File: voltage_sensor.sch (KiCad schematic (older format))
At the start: 20 parts, among them K1 REF, P1 Input, P2 CONN_4, P3 CONN_2, U1 REF5020, U2 LT6011, U3 ADUM5401, U4 MCP3550

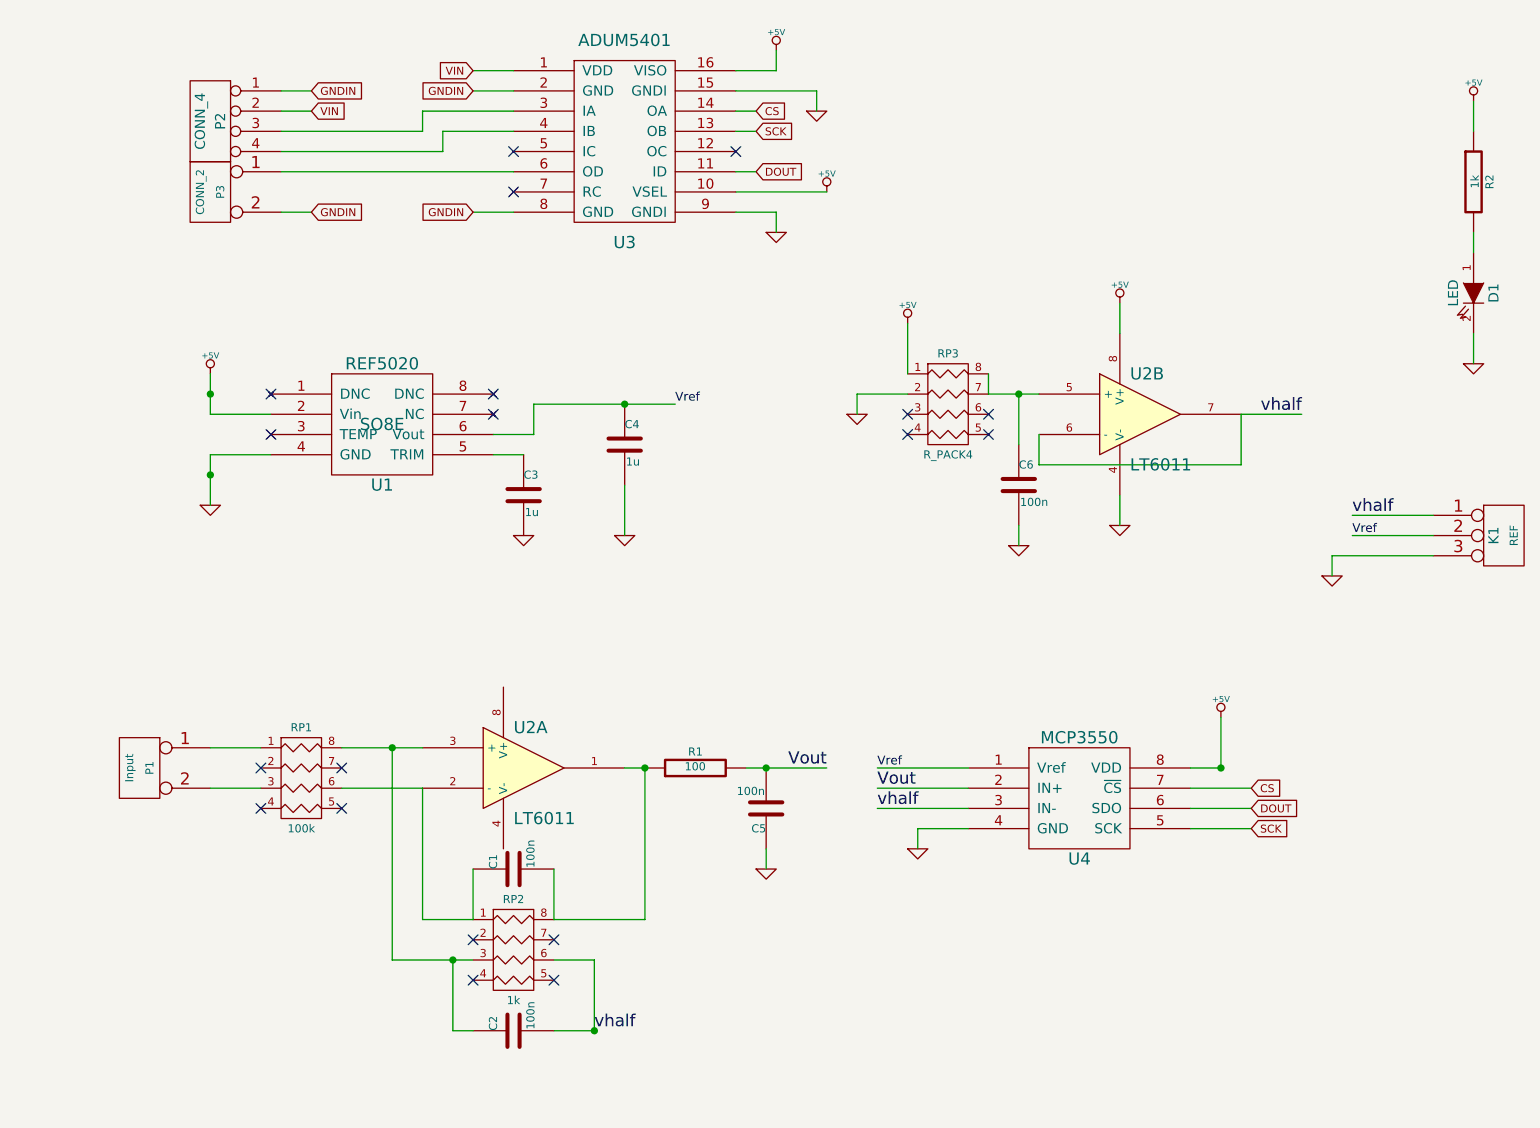
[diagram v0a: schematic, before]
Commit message: Started routing board
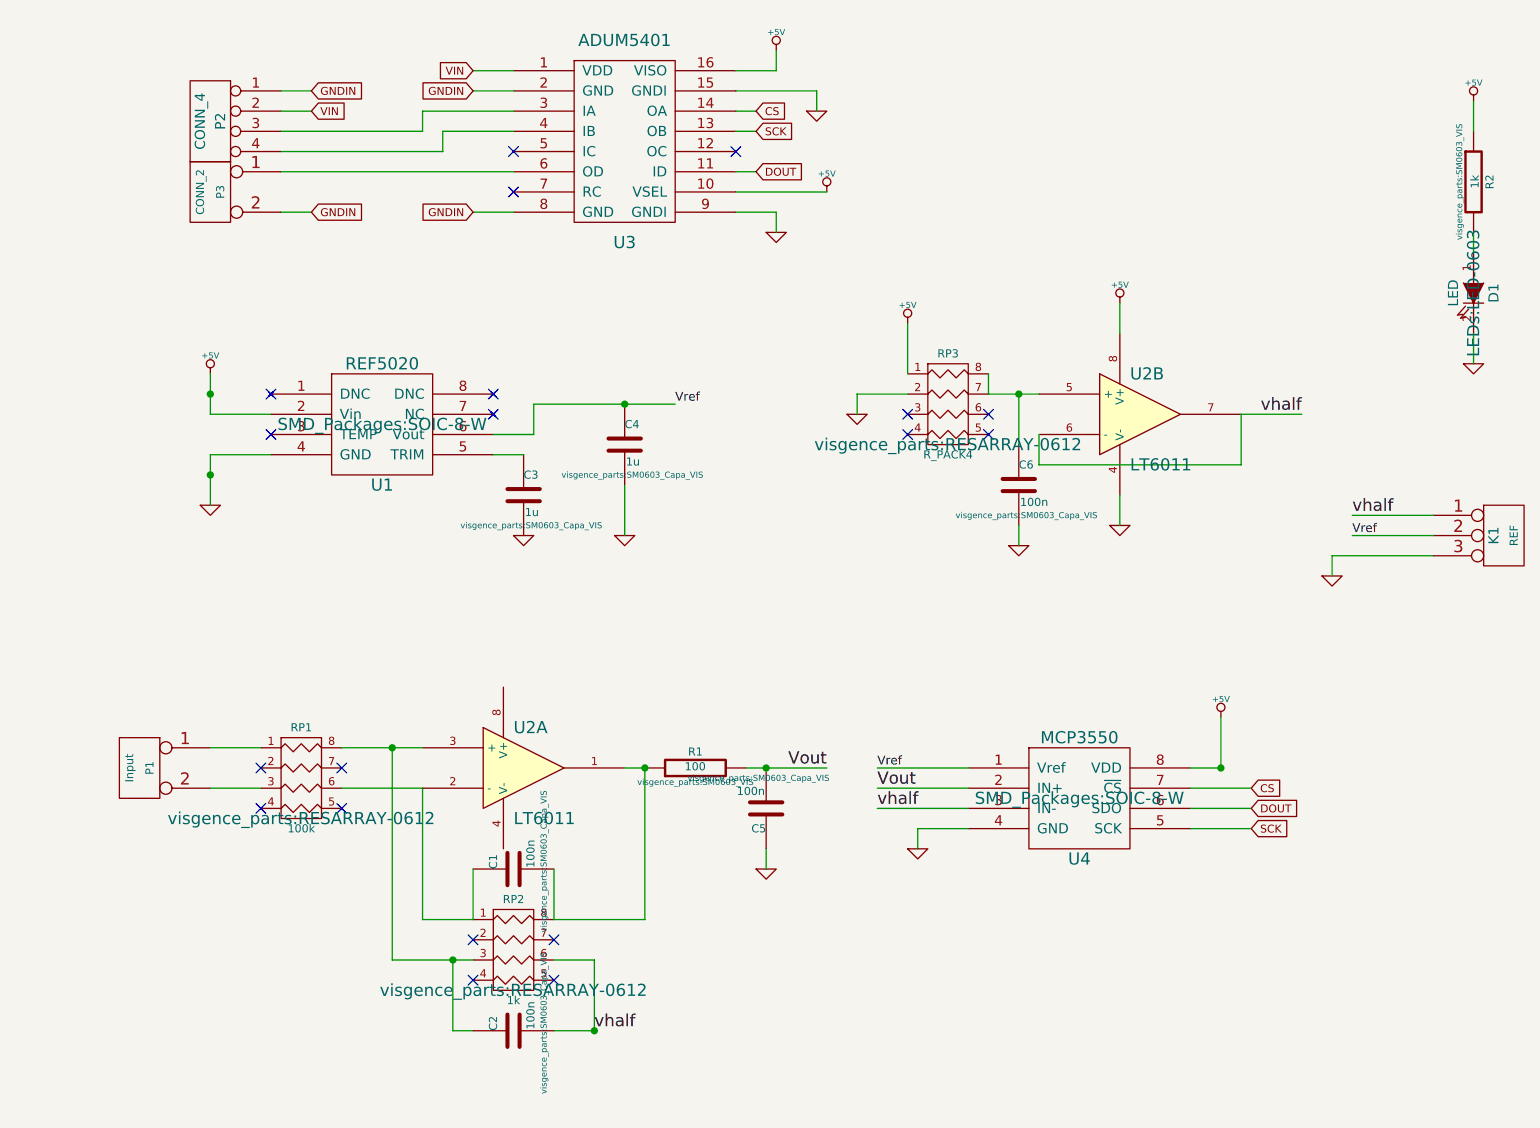
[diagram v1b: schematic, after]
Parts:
- C1, C2, C3, C4, C5, C6: footprint ~ -> visgence_parts:SM0603_Capa_VIS
- D1: footprint ~ -> LEDs:LED-0603
- K1: footprint (none) -> Pin_Headers:Pin_Header_Straight_1x03
- P1: footprint (none) -> Connect:bornier2
- P2: footprint (none) -> visgence_parts:Term3.5-4
- P3: footprint (none) -> visgence_parts:Term3.5-2
- R1, R2: footprint ~ -> visgence_parts:SM0603_VIS
- RP1, RP2, RP3: footprint ~ -> visgence_parts:RESARRAY-0612
- U1: footprint SO8E -> SMD_Packages:SOIC-8-W
- U2: footprint (none) -> SMD_Packages:SOIC-8-W
- U3: footprint (none) -> SMD_Packages:SO-16-W
- U4: footprint ~ -> SMD_Packages:SOIC-8-W
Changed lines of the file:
@@
 F 0 "C4" H 4050 3300 40  0000 L CNN
 F 1 "1u" H 4056 3115 40  0000 L CNN
-F 2 "~" H 4088 3050 30  0000 C CNN
+F 2 "visgence_parts:SM0603_Capa_VIS" H 4088 3050 30  0000 C CNN
 F 3 "~" H 4050 3200 60  0000 C CNN
 	1    4050 3200
@@
 F 0 "RP3" H 5650 3650 40  0000 C CNN
 F 1 "R_PACK4" H 5650 3150 40  0000 C CNN
-F 2 "~" H 5650 3200 60  0000 C CNN
+F 2 "visgence_parts:RESARRAY-0612" H 5650 3200 60  0000 C CNN
 F 3 "~" H 5650 3200 60  0000 C CNN
 	1    5650 3200
@@
 F 0 "C6" H 6000 3500 40  0000 L CNN
 F 1 "100n" H 6006 3315 40  0000 L CNN
-F 2 "~" H 6038 3250 30  0000 C CNN
+F 2 "visgence_parts:SM0603_Capa_VIS" H 6038 3250 30  0000 C CNN
 F 3 "~" H 6000 3400 60  0000 C CNN
 	1    6000 3400
@@
 F 0 "RP1" H 2450 5500 40  0000 C CNN
 F 1 "100k" H 2450 5000 40  0000 C CNN
-F 2 "~" H 2450 5050 60  0000 C CNN
+F 2 "visgence_parts:RESARRAY-0612" H 2450 5050 60  0000 C CNN
 F 3 "~" H 2450 5050 60  0000 C CNN
 	1    2450 5050
@@
 F 0 "RP2" H 3500 6350 40  0000 C CNN
 F 1 "1k" H 3500 5850 40  0000 C CNN
-F 2 "~" H 3500 5900 60  0000 C CNN
+F 2 "visgence_parts:RESARRAY-0612" H 3500 5900 60  0000 C CNN
 F 3 "~" H 3500 5900 60  0000 C CNN
 	1    3500 5900
@@
 F 0 "C1" H 3500 5400 40  0000 L CNN
 F 1 "100n" H 3506 5215 40  0000 L CNN
-F 2 "~" H 3538 5150 30  0000 C CNN
+F 2 "visgence_parts:SM0603_Capa_VIS" H 3538 5150 30  0000 C CNN
 F 3 "~" H 3500 5300 60  0000 C CNN
 	1    3500 5300
@@
 F 0 "C2" H 3500 6200 40  0000 L CNN
 F 1 "100n" H 3506 6015 40  0000 L CNN
-F 2 "~" H 3538 5950 30  0000 C CNN
+F 2 "visgence_parts:SM0603_Capa_VIS" H 3538 5950 30  0000 C CNN
 F 3 "~" H 3500 6100 60  0000 C CNN
 	1    3500 6100
@@
 F 0 "R1" V 4480 4800 40  0000 C CNN
 F 1 "100" V 4407 4801 40  0000 C CNN
-F 2 "~" V 4330 4800 30  0000 C CNN
+F 2 "visgence_parts:SM0603_VIS" V 4330 4800 30  0000 C CNN
 F 3 "~" H 4400 4800 30  0000 C CNN
 	1    4400 4800
@@
 F 0 "C5" H 4750 5100 40  0000 L CNN
 F 1 "100n" H 4756 4915 40  0000 L CNN
-F 2 "~" H 4788 4850 30  0000 C CNN
+F 2 "visgence_parts:SM0603_Capa_VIS" H 4788 4850 30  0000 C CNN
 F 3 "~" H 4750 5000 60  0000 C CNN
 	1    4750 5000
@@
 F 0 "P1" V 1600 4800 40  0000 C CNN
 F 1 "Input" V 1700 4800 40  0000 C CNN
-F 2 "" H 1650 4800 60  0000 C CNN
+F 2 "Connect:bornier2" H 1650 4800 60  0001 C CNN
 F 3 "" H 1650 4800 60  0000 C CNN
 	1    1650 4800
@@
 F 0 "D1" H 8250 2550 50  0000 C CNN
 F 1 "LED" H 8250 2350 50  0000 C CNN
-F 2 "~" H 8250 2450 60  0000 C CNN
+F 2 "LEDs:LED-0603" H 8250 2450 60  0000 C CNN
 F 3 "~" H 8250 2450 60  0000 C CNN
 	1    8250 2450
@@
 F 0 "R2" V 8330 1900 40  0000 C CNN
 F 1 "1k" V 8257 1901 40  0000 C CNN
-F 2 "~" V 8180 1900 30  0000 C CNN
+F 2 "visgence_parts:SM0603_VIS" V 8180 1900 30  0000 C CNN
 F 3 "~" H 8250 1900 30  0000 C CNN
 	1    8250 1900
@@
 F 0 "K1" V 8350 3650 50  0000 C CNN
 F 1 "REF" V 8450 3650 40  0000 C CNN
-F 2 "" H 8400 3650 60  0000 C CNN
+F 2 "Pin_Headers:Pin_Header_Straight_1x03" H 8400 3650 60  0001 C CNN
 F 3 "" H 8400 3650 60  0000 C CNN
 	1    8400 3650
@@
 F 0 "U2" H 6550 3250 60  0000 L CNN
 F 1 "LT6011" H 6550 2800 60  0000 L CNN
-F 2 "" H 6600 3050 60  0000 C CNN
+F 2 "SMD_Packages:SOIC-8-W" H 6600 3050 60  0001 C CNN
 F 3 "" H 6600 3050 60  0000 C CNN
 	2    6600 3050
@@
 F 0 "U1" H 2850 2800 60  0000 C CNN
 F 1 "REF5020" H 2850 3400 60  0000 C CNN
-F 2 "SO8E" H 2850 3100 60  0000 C CNN
+F 2 "SMD_Packages:SOIC-8-W" H 2850 3100 60  0000 C CNN
 F 3 "~" H 2850 3100 60  0000 C CNN
 	1    2850 3100
@@
 F 0 "U2" H 3500 5000 60  0000 L CNN
 F 1 "LT6011" H 3500 4550 60  0000 L CNN
-F 2 "" H 3550 4800 60  0000 C CNN
+F 2 "SMD_Packages:SOIC-8-W" H 3550 4800 60  0001 C CNN
 F 3 "" H 3550 4800 60  0000 C CNN
 	1    3550 4800
@@
 F 0 "U4" H 6300 4650 60  0000 C CNN
 F 1 "MCP3550" H 6300 5250 60  0000 C CNN
-F 2 "~" H 6300 4950 60  0000 C CNN
+F 2 "SMD_Packages:SOIC-8-W" H 6300 4950 60  0000 C CNN
 F 3 "~" H 6300 4950 60  0000 C CNN
 	1    6300 4950
@@
 F 0 "C3" H 3550 3550 40  0000 L CNN
 F 1 "1u" H 3556 3365 40  0000 L CNN
-F 2 "~" H 3588 3300 30  0000 C CNN
+F 2 "visgence_parts:SM0603_Capa_VIS" H 3588 3300 30  0000 C CNN
 F 3 "~" H 3550 3450 60  0000 C CNN
 	1    3550 3450
@@
 F 0 "U3" H 4050 1200 60  0000 C CNN
 F 1 "ADUM5401" H 4050 2200 60  0000 C CNN
-F 2 "" H 4050 1600 60  0000 C CNN
+F 2 "SMD_Packages:SO-16-W" H 4050 1600 60  0001 C CNN
 F 3 "" H 4050 1600 60  0000 C CNN
 	1    4050 1700
@@
 F 0 "P2" V 1950 1600 50  0000 C CNN
 F 1 "CONN_4" V 2050 1600 50  0000 C CNN
-F 2 "" H 2000 1600 60  0000 C CNN
+F 2 "visgence_parts:Term3.5-4" H 2000 1600 60  0001 C CNN
 F 3 "" H 2000 1600 60  0000 C CNN
 	1    2000 1600
@@
 F 0 "P3" V 1950 1950 40  0000 C CNN
 F 1 "CONN_2" V 2050 1950 40  0000 C CNN
-F 2 "" H 2000 1950 60  0000 C CNN
+F 2 "visgence_parts:Term3.5-2" H 2000 1950 60  0001 C CNN
 F 3 "" H 2000 1950 60  0000 C CNN
 	1    2000 1950

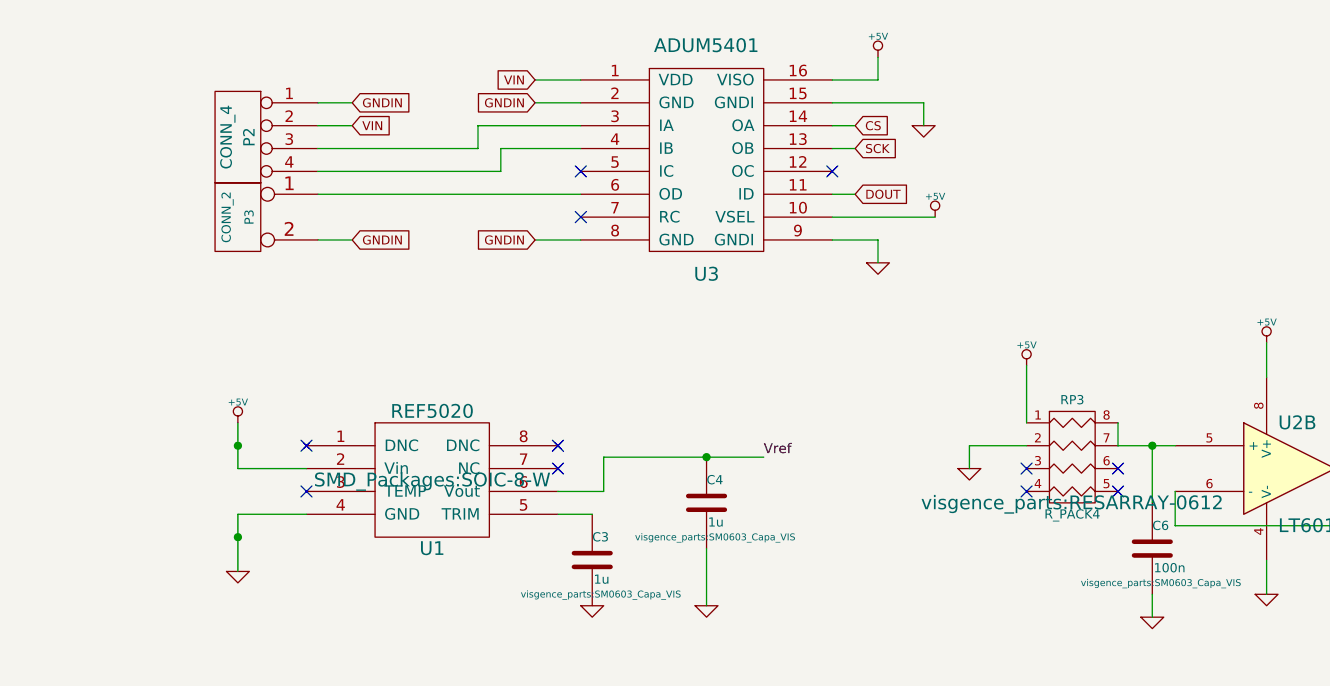
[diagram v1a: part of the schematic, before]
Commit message: Added filter caps
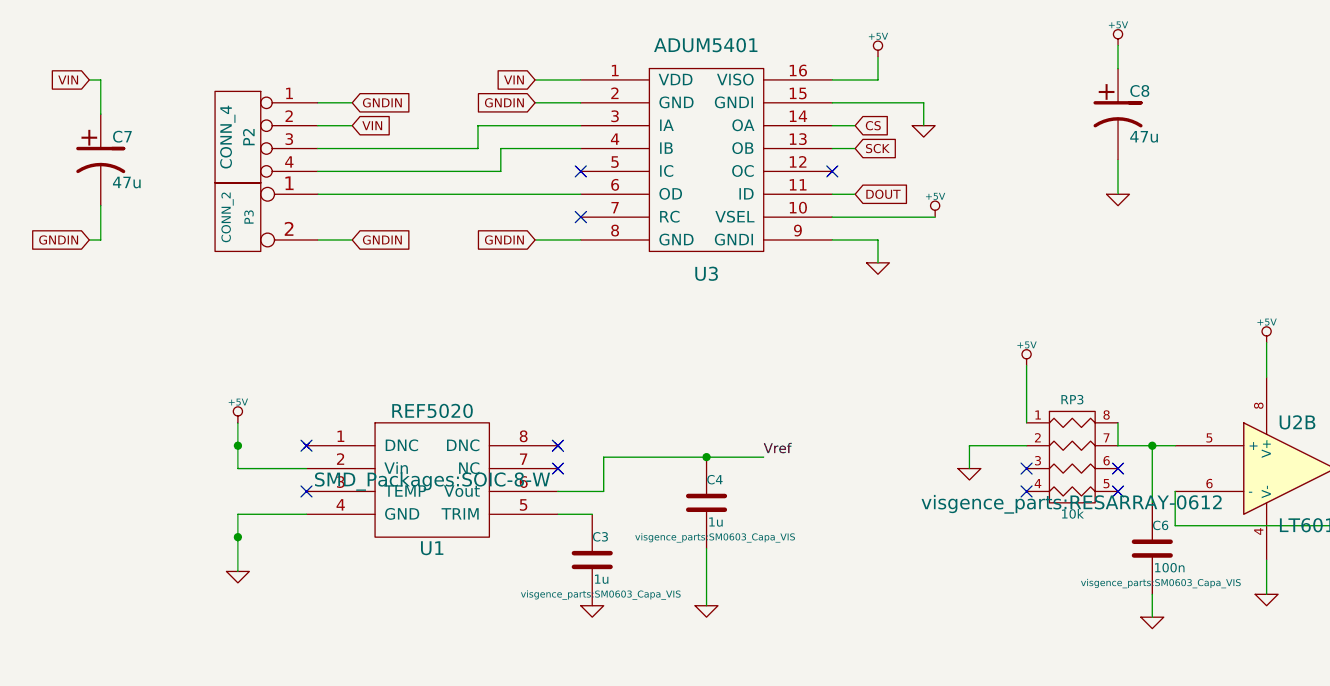
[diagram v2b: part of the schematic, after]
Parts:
- added C7, C8: 47u, visgence_parts:SM1206POL_VIS, symbol CP1
- RP3: value R_PACK4 -> 10k
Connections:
- net +5V: now also C8.1
- net GND: now also C8.2
- net GNDIN: now also C7.2
- net VIN: now also C7.1
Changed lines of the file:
@@
 P 5650 3200
 F 0 "RP3" H 5650 3650 40  0000 C CNN
-F 1 "R_PACK4" H 5650 3150 40  0000 C CNN
+F 1 "10k" H 5650 3150 40  0000 C CNN
 F 2 "visgence_parts:RESARRAY-0612" H 5650 3200 60  0000 C CNN
 F 3 "~" H 5650 3200 60  0000 C CNN
@@
 	3300 1350 3500 1350
 NoConn ~ 3500 1750
+$Comp
+L CP1 C8
+U 1 1 53EC4C40
+P 5850 1500
+F 0 "C8" H 5900 1600 50  0000 L CNN
+F 1 "47u" H 5900 1400 50  0000 L CNN
+F 2 "visgence_parts:SM1206POL_VIS" H 5850 1500 60  0001 C CNN
+F 3 "" H 5850 1500 60  0000 C CNN
+	1    5850 1500
+	1    0    0    -1
+$EndComp
+$Comp
+L +5V #PWR020
+U 1 1 53EC4C83
+P 5850 1200
+F 0 "#PWR020" H 5850 1290 20  0001 C CNN
+F 1 "+5V" H 5850 1290 30  0000 C CNN
+F 2 "" H 5850 1200 60  0000 C CNN
+F 3 "" H 5850 1200 60  0000 C CNN
+	1    5850 1200
+	1    0    0    -1
+$EndComp
+$Comp
+L GND #PWR021
+U 1 1 53EC4CA4
+P 5850 1850
+F 0 "#PWR021" H 5850 1850 30  0001 C CNN
+F 1 "GND" H 5850 1780 30  0001 C CNN
+F 2 "" H 5850 1850 60  0000 C CNN
+F 3 "" H 5850 1850 60  0000 C CNN
+	1    5850 1850
+	1    0    0    -1
+$EndComp
+Wire Wire Line
+	5850 1300 5850 1200
+Wire Wire Line
+	5850 1700 5850 1850
+$Comp
+L CP1 C7
+U 1 1 53EC4E8F
+P 1400 1700
+F 0 "C7" H 1450 1800 50  0000 L CNN
+F 1 "47u" H 1450 1600 50  0000 L CNN
+F 2 "visgence_parts:SM1206POL_VIS" H 1400 1700 60  0001 C CNN
+F 3 "" H 1400 1700 60  0000 C CNN
+	1    1400 1700
+	1    0    0    -1
+$EndComp
+Text GLabel 1350 2050 0    39   Input ~ 0
+GNDIN
+Text GLabel 1350 1350 0    39   Input ~ 0
+VIN
+Wire Wire Line
+	1350 1350 1400 1350
+Wire Wire Line
+	1400 1350 1400 1500
+Wire Wire Line
+	1350 2050 1400 2050
+Wire Wire Line
+	1400 2050 1400 1900
 $EndSCHEMATC
